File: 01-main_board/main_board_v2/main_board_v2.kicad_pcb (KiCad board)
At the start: 4 copper layers, 94.9 x 62.8 mm, 159 parts, among them IC1 MAX6105EUR+T, IC10 ESP32-S3, IC11 LT3973EMSE-5#PBF, IC2 LP5907MFX-2.5_NOPB, IC3 TS3USB30EDGSR, IC4 SPX3819S-L_TR, IC5 INA827AIDGK, IC6 AD7175-8BCPZ-RL7, IC7 INA827AIDGK, IC8 AD8591ARTZ-REEL7, IC9 LSF0108PWR, J1 Mezzanine Edge, J4 DB44 (Analog | Digital), T1 749013011, U1 Teensy4.1, U2 AD5689RARUZ-RL7, U3 MCP2562FD-E/SN, U4 TPS2115APWR, Y1 ECS-400-10-37B2-CKY-TR, Y2 ECS-.327-12.5-34B-TR

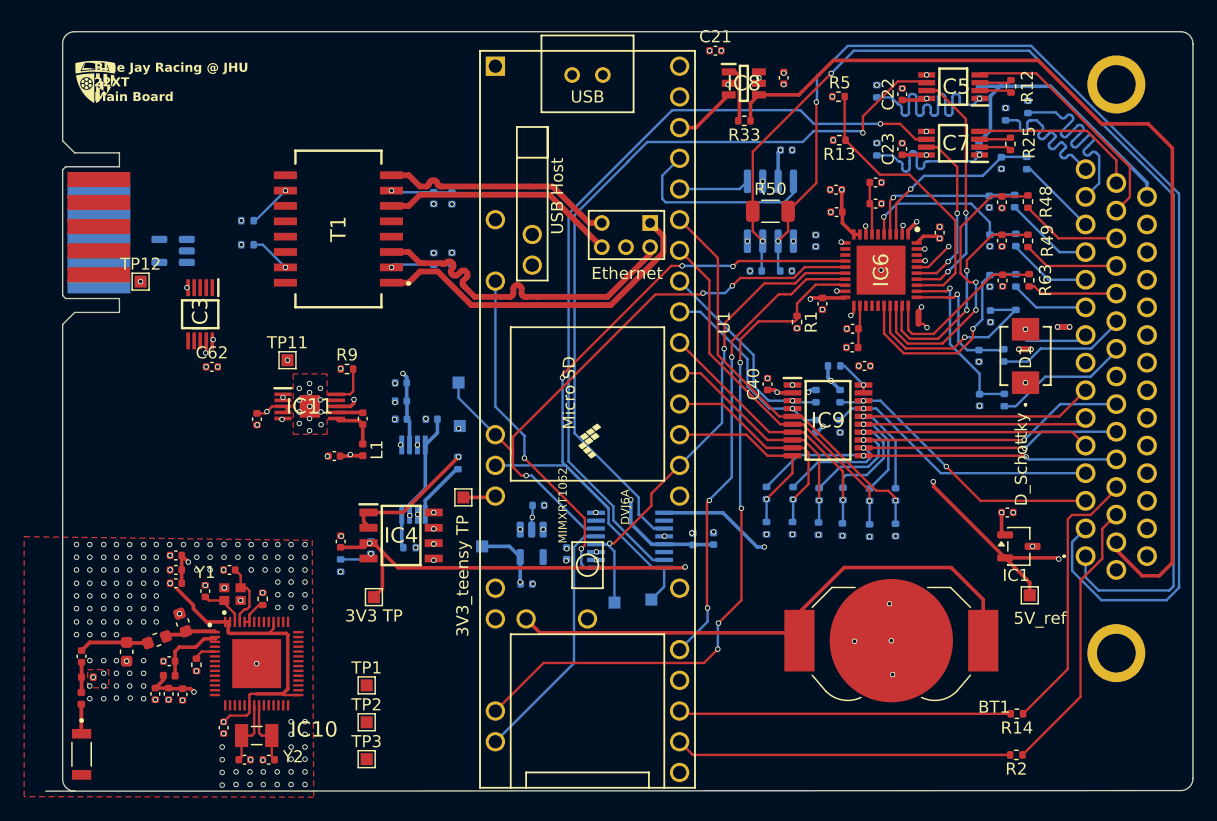
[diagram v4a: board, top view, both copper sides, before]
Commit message: finished layout, resolved drc errors, need to resolve warnings and get checked
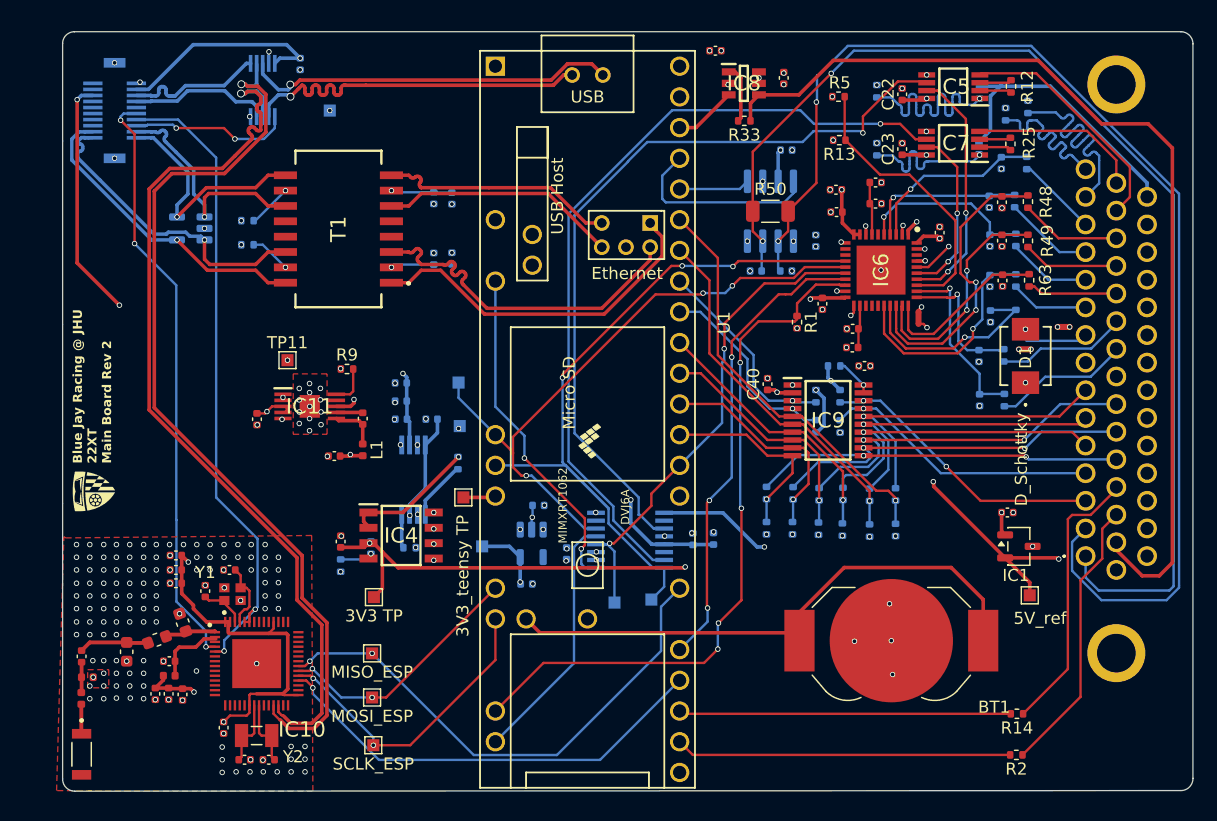
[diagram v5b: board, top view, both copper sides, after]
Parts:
- removed J1: Mezzanine Edge, 22XT_Main:Double Sided Mezzanine Card Edge_Edge Side
- removed R100, R101: 10k, Resistor_SMD:R_0402_1005Metric
- added J2: DF12NB-20DS-0.5V_51_, 22XT_Main:DF12NB20DS05V51, B.Cu at (48.7, 27.2)
- C62, IC3, TP12: moved to B.Cu
- moved G*** 33.9 mm to (47.0, 58.7), turned to 90 degrees
- moved C62 26.1 mm to (64.0, 23.4), turned to 90 degrees
- moved TP12 21.1 mm to (66.5, 27.2), turned to 180 degrees
- moved IC3 19.3 mm to (61.0, 25.5), turned to 90 degrees
- moved TP1 2.69 mm to (70.0, 72.1)
- moved D2 2.37 mm to (55.0, 37.0)
- moved TP2 2.10 mm to (70.0, 75.8)
- moved TP3 1.27 mm to (70.1, 79.7)
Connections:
- IC10 pad 4: unconnected-(IC10-CHIP_PU-Pad4) -> ESP_RESET_CONTROL
- IC10 pad 5: Net-(IC10-GPIO0) -> ESP_BOOT_CONTROL
- IC10 pad 51: Net-(IC10-GPIO45) -> ESP_BOOT_CONTROL
- IC10 pad 52: Net-(IC10-GPIO45) -> ESP_BOOT_CONTROL
- IC3 pad 1: usb_mux_s -> USB_MUX_CONTROL
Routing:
- net 5V_usb: track 9.06 -> 98.7 mm, vias 4 -> 3
- net usb_esp-: track 0.00 -> 75.2 mm, vias 0 -> 1
- net usb_esp+: track 0.00 -> 75.2 mm, vias 0 -> 1
- net ESP_BOOT_CONTROL: track 0.00 -> 53.8 mm, vias 0 -> 2
- net ESP_RESET_CONTROL: track 0.00 -> 48.9 mm, vias 0 -> 3
- net MISO_ESP: track 0.00 -> 43.3 mm, vias 0 -> 2
- net CS_ESP: track 0.00 -> 37.3 mm, vias 0 -> 1
- net usb_teensy-: track 0.00 -> 31.0 mm, vias 0 -> 1
- net usb_teensy+: track 0.00 -> 30.8 mm, vias 0 -> 1
- net RX+: track 0.00 -> 25.6 mm, vias 0 -> 1
- net RX-: track 0.00 -> 25.5 mm, vias 0 -> 1
- net SCLK_ESP: track 0.00 -> 25.4 mm, vias 0 -> 2
- net MOSI_ESP: track 0.00 -> 21.1 mm, vias 0 -> 2
- net 3V3: track 109.1 -> 129.2 mm, vias 6 -> 8
- net TX-: track 0.00 -> 19.9 mm, vias 0 -> 1
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- added copper zone on In2.Cu, net GNDD
- removed copper zone on In2.Cu, net 5V_usb
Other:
- board size 94.9 x 62.8 mm -> 93.5 x 62.8 mm
- board text added: "Blue Jay Racing @ JHU 22XT Main Board Rev 2"
- board text removed: "Blue Jay Racing @ JHU 22XT Main Board"

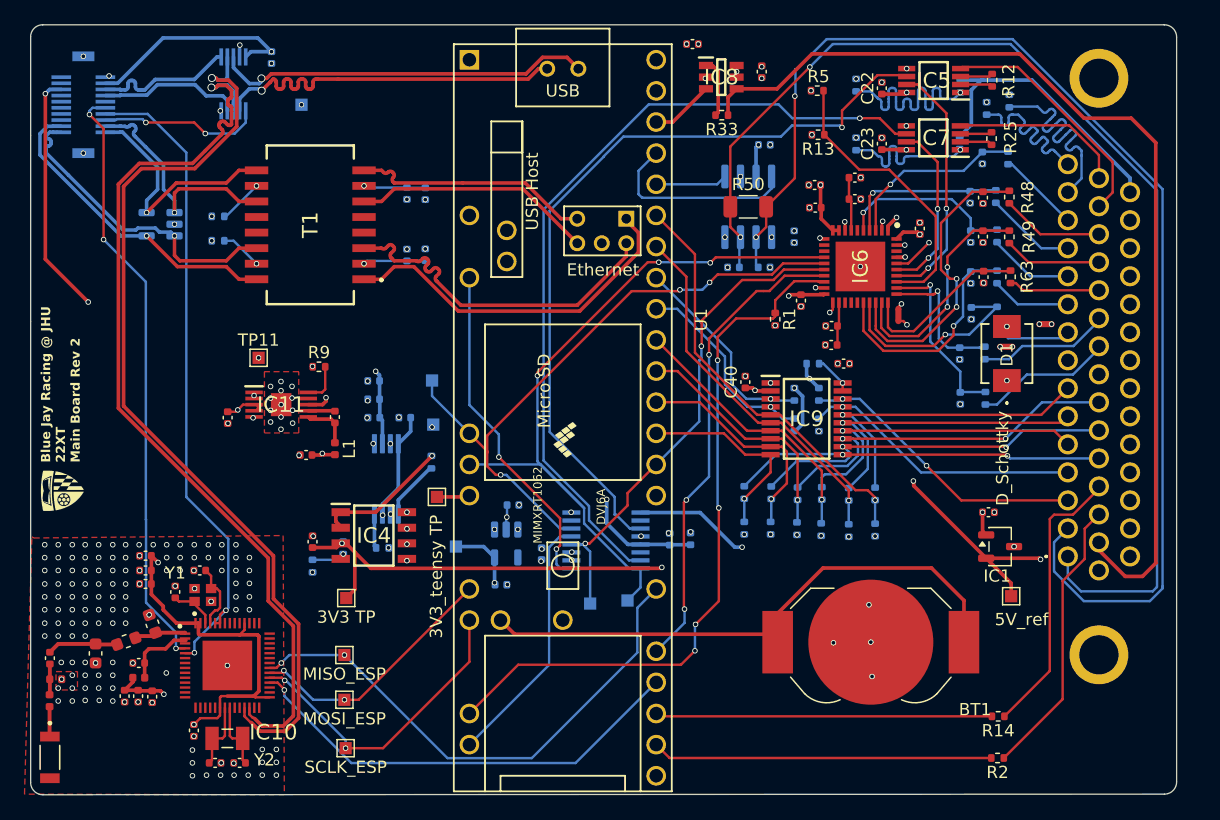
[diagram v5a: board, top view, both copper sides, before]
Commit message: resolved silkscreen issues, tied gpio45 to gnd
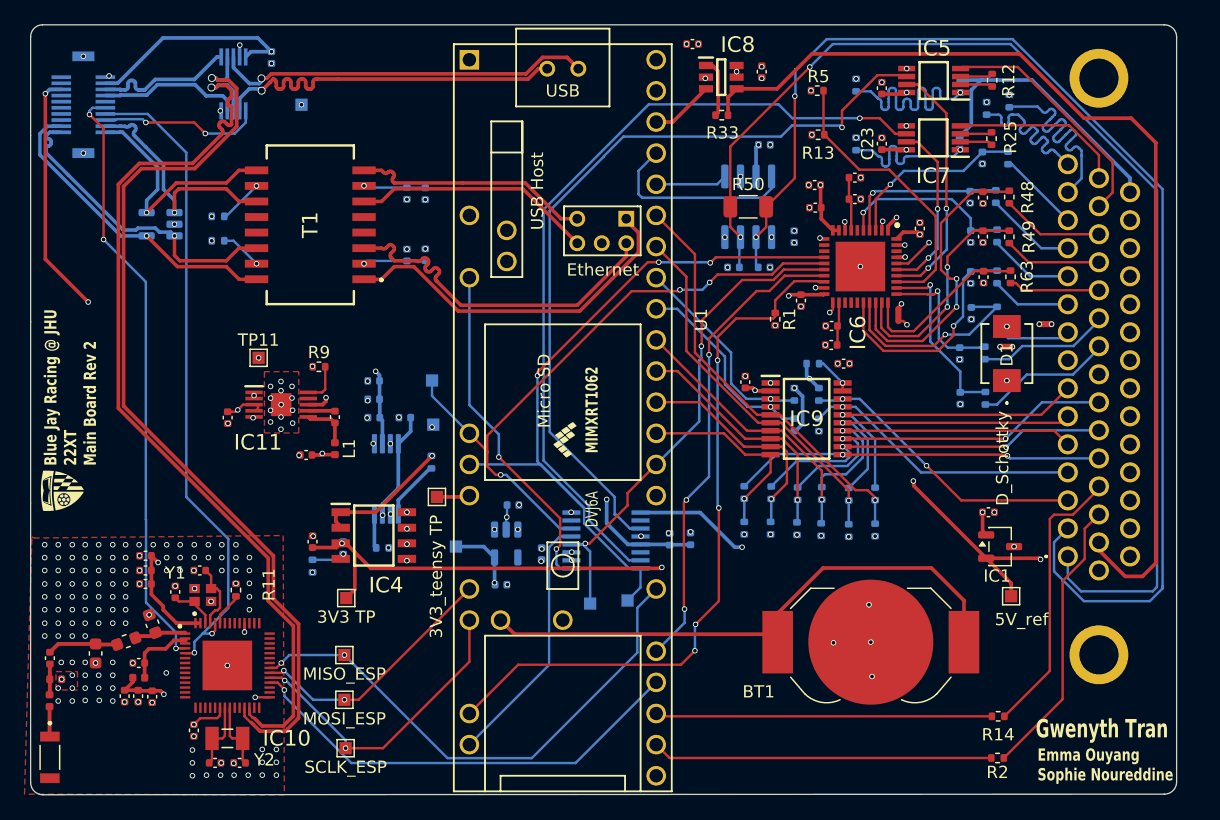
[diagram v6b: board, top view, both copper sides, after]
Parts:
- added R11: 10k, Resistor_SMD:R_0402_1005Metric, F.Cu at (61.1, 66.8)
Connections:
- IC10 pad 51: ESP_BOOT_CONTROL -> Net-(IC10-GPIO45)
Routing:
- net 3V3: track 129.2 -> 114.2 mm, vias 8 -> 10
- net Net-(IC10-GPIO45): track 0.00 -> 2.73 mm
- net GNDD: vias 166 -> 164
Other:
- board text added: "Emma Ouyang Sophie Noureddine"
- board text added: "Gwenyth Tran"

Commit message: dimensions finalized
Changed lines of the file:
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@@
 	)
 	(gr_line
-		(start 137.9 82.449999)
-		(end 137.899949 21.67995)
-		(stroke
-			(width 0.05)
-			(type default)
-		)
-		(layer "Edge.Cuts")
-	)
-	(gr_arc
-		(start 136.9 20.67995)
-		(mid 137.607089 20.972846)
-		(end 137.9 21.67995)
+		(start 137.9 82.45)
+		(end 137.899949 21.7)
+		(stroke
+			(width 0.05)
+			(type default)
+		)
+		(layer "Edge.Cuts")
+	)
+	(gr_arc
+		(start 136.9 20.7)
+		(mid 137.607124 20.99289)
+		(end 137.9 21.7)
 		(stroke
 			(width 0.05)
@@
 	)
 	(gr_line
-		(start 44.4 21.657103)
+		(start 44.4 21.677153)
 		(end 44.4 29.7)
 		(stroke
@@
 	)
 	(gr_line
-		(start 136.9 20.67995)
-		(end 45.377104 20.67995)
+		(start 136.9 20.7)
+		(end 45.377104 20.7)
 		(stroke
 			(width 0.05)
@@
 	)
 	(gr_arc
-		(start 44.4 21.657103)
-		(mid 44.68617 20.966154)
-		(end 45.377104 20.67995)
+		(start 44.4 21.677153)
+		(mid 44.686186 20.986236)
+		(end 45.377104 20.7)
 		(stroke
 			(width 0.05)
@@
 		(layer "Dwgs.User")
 		(pts
-			(xy 136.9 20.67995) (xy 136.9 83.45)
-		)
-		(height 6.3)
+			(xy 136.9 20.7) (xy 136.9 83.45)
+		)
+		(height 6.4)
 		(orientation 1)
 		(format
@@
 			(keep_text_aligned yes)
 		)
-		(gr_text "62.77"
-			(at 142.05 52.064975 90)
+		(gr_text "62.75"
+			(at 142.15 52.075 90)
 			(layer "Dwgs.User")
 			(effects

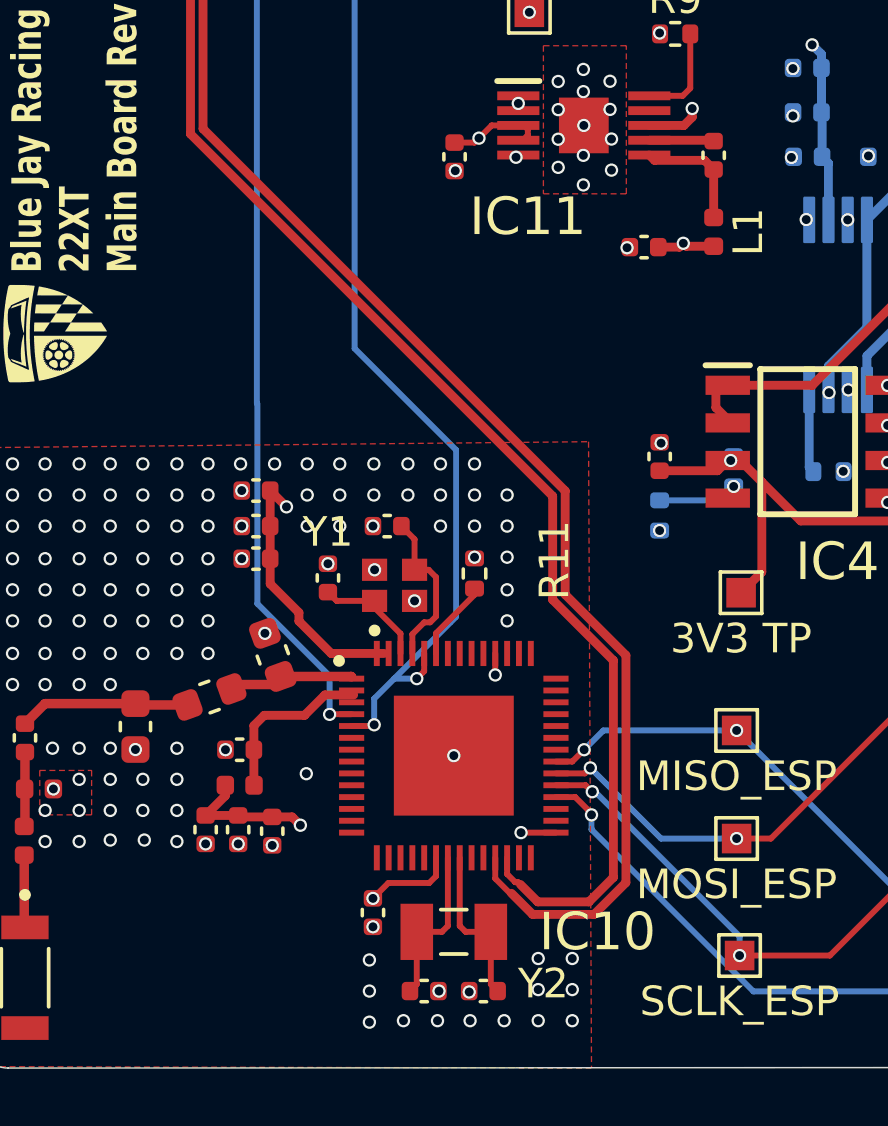
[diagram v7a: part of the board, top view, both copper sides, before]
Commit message: added gpio3 tp
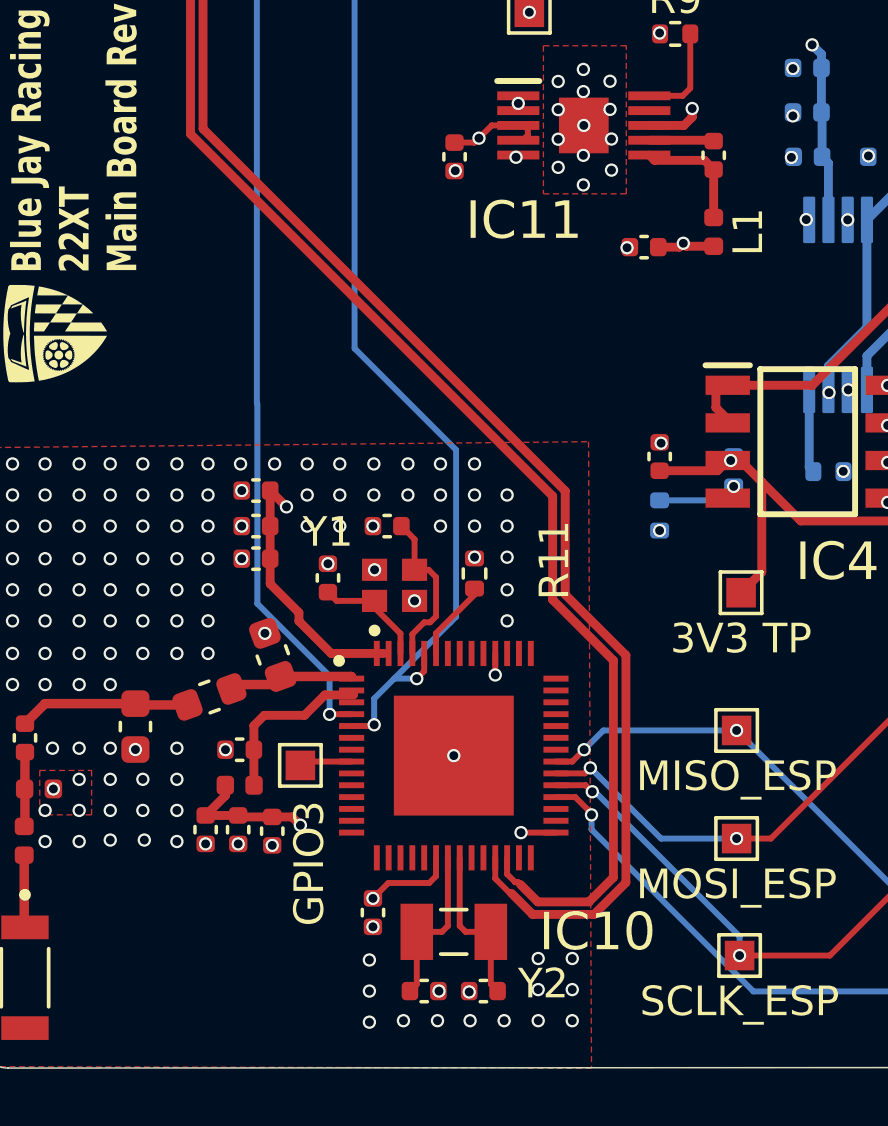
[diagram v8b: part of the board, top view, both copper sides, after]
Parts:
- added TP14: GPIO3, TestPoint:TestPoint_Pad_1.0x1.0mm, F.Cu at (55.3, 73.3)
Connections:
- IC10 pad 8: unconnected-(IC10-GPIO3-Pad8) -> Net-(IC10-GPIO3)
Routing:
- net Net-(IC10-GPIO3): track 0.00 -> 1.78 mm
- net GNDD: vias 164 -> 163
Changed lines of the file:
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@@
 	(net 137 "unconnected-(IC10-SPIWP-Pad31)")
 	(net 138 "unconnected-(IC10-GPIO38-Pad43)")
-	(net 139 "unconnected-(IC10-GPIO3-Pad8)")
+	(net 139 "Net-(IC10-GPIO3)")
 	(net 140 "unconnected-(IC10-GPIO11-Pad16)")
 	(net 141 "unconnected-(IC10-U0TXD-Pad49)")
@@
 		(tags "Integrated Circuit")
 		(property "Reference" "IC11"
-			(at -1.89 3.079 0)
+			(at -2.02 3.209 0)
 			(layer "F.SilkS")
 			(effects
@@
 		)
 		(embedded_fonts no)
-		(model "LT3973EMSE-5#PBF.stp"
+		(model "C:/Users/notlu/OneDrive/Desktop/22xt_kicad/01-main_board/00-3dmodels/LT3973EMSE-5#PBF.stp"
 			(offset
 				(xyz 0 0 0.5299999634)
@@
 			(size 0.2 0.85)
 			(layers "F.Cu" "F.Mask" "F.Paste")
-			(net 139 "unconnected-(IC10-GPIO3-Pad8)")
+			(net 139 "Net-(IC10-GPIO3)")
 			(pinfunction "GPIO3")
-			(pintype "passive+no_connect")
+			(pintype "passive")
 		)
 		(pad "9" smd rect
@@
 		)
 	)
+	(footprint "TestPoint:TestPoint_Pad_1.0x1.0mm"
+		(layer "F.Cu")
+		(at 55.27 73.28)
+		(descr "SMD rectangular pad as test Point, square 1.0mm side length")
+		(tags "test point SMD pad rectangle square")
+		(property "Reference" "TP14"
+			(at 0 -1.448 0)
+			(layer "F.SilkS")
+			(hide yes)
+			(effects
+				(font
+					(size 1 1)
+					(thickness 0.15)
+				)
+			)
+		)
+		(property "Value" "GPIO3"
+			(at 0.3 3.31 90)
+			(layer "F.SilkS")
+			(effects
+				(font
+					(size 1 1)
+					(thickness 0.15)
+				)
+			)
+		)
+		(property "Datasheet" "~"
+			(at 0 0 0)
+			(unlocked yes)
+			(layer "F.Fab")
+			(hide yes)
+			(effects
+				(font
+					(size 1.27 1.27)
+					(thickness 0.15)
+				)
+			)
+		)
+		(property "Description" "test point"
+			(at 0 0 0)
+			(unlocked yes)
+			(layer "F.Fab")
+			(hide yes)
+			(effects
+				(font
+					(size 1.27 1.27)
+					(thickness 0.15)
+				)
+			)
+		)
+		(property ki_fp_filters "Pin* Test*")
+		(sheetname "/ESP32S3/")
+		(sheetfile "esp32s3.kicad_sch")
+		(attr exclude_from_pos_files)
+		(fp_line
+			(start -0.7 -0.7)
+			(end 0.7 -0.7)
+			(stroke
+				(width 0.12)
+				(type solid)
+			)
+			(layer "F.SilkS")
+		)
+		(fp_line
+			(start -0.7 0.7)
+			(end -0.7 -0.7)
+			(stroke
+				(width 0.12)
+				(type solid)
+			)
+			(layer "F.SilkS")
+		)
+		(fp_line
+			(start 0.7 -0.7)
+			(end 0.7 0.7)
+			(stroke
+				(width 0.12)
+				(type solid)
+			)
+			(layer "F.SilkS")
+		)
+		(fp_line
+			(start 0.7 0.7)
+			(end -0.7 0.7)
+			(stroke
+				(width 0.12)
+				(type solid)
+			)
+			(layer "F.SilkS")
+		)
+		(fp_line
+			(start -1 -1)
+			(end -1 1)
+			(stroke
+				(width 0.05)
+				(type solid)
+			)
+			(layer "F.CrtYd")
+		)
+		(fp_line
+			(start -1 -1)
+			(end 1 -1)
+			(stroke
+				(width 0.05)
+				(type solid)
+			)
+			(layer "F.CrtYd")
+		)
+		(fp_line
+			(start 1 1)
+			(end -1 1)
+			(stroke
+				(width 0.05)
+				(type solid)
+			)
+			(layer "F.CrtYd")
+		)
+		(fp_line
+			(start 1 1)
+			(end 1 -1)
+			(stroke
+				(width 0.05)
+				(type solid)
+			)
+			(layer "F.CrtYd")
+		)
+		(pad "1" smd rect
+			(at 0 0)
+			(size 1 1)
+			(layers "F.Cu" "F.Mask")
+			(net 139 "Net-(IC10-GPIO3)")
+			(pinfunction "1")
+			(pintype "passive")
+		)
+		(embedded_fonts no)
+	)
 	(footprint "Capacitor_SMD:C_0402_1005Metric"
 		(layer "F.Cu")
@@
 		)
 		(embedded_fonts no)
-		(model "DF12NB-20DS-0.5V_51_.stp"
+		(model "C:/Users/notlu/OneDrive/Desktop/22xt_kicad/01-main_board/00-3dmodels/DF12NB-20DS-0.5V_51_.stp"
 			(offset
 				(xyz 0 0 0)
@@
 		(tags "Integrated Circuit")
 		(property "Reference" "IC3"
-			(at 0 -2.95 270)
+			(at -2.26 -3.36 270)
 			(layer "B.SilkS")
 			(effects
@@
 	)
 	(via
-		(at 55.47 73.56)
-		(size 0.45)
-		(drill 0.3)
-		(layers "F.Cu" "B.Cu")
-		(net 44)
-	)
-	(via
 		(at 45.55 64.15)
 		(size 0.45)
@@
 	)
 	(segment
+		(start 57 73.15)
+		(end 55.4 73.15)
+		(width 0.2)
+		(layer "F.Cu")
+		(net 139)
+	)
+	(segment
+		(start 55.4 73.15)
+		(end 55.27 73.28)
+		(width 0.2)
+		(layer "F.Cu")
+		(net 139)
+	)
+	(segment
